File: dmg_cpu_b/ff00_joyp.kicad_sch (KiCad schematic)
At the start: 59 parts, among them P10 PAD_BIDIR_ENA_PU, P11 PAD_BIDIR_ENA_PU, P12 PAD_BIDIR_ENA_PU, P13 PAD_BIDIR_ENA_PU, P14 PAD_OUT_DIFF, P15 PAD_OUT_DIFF

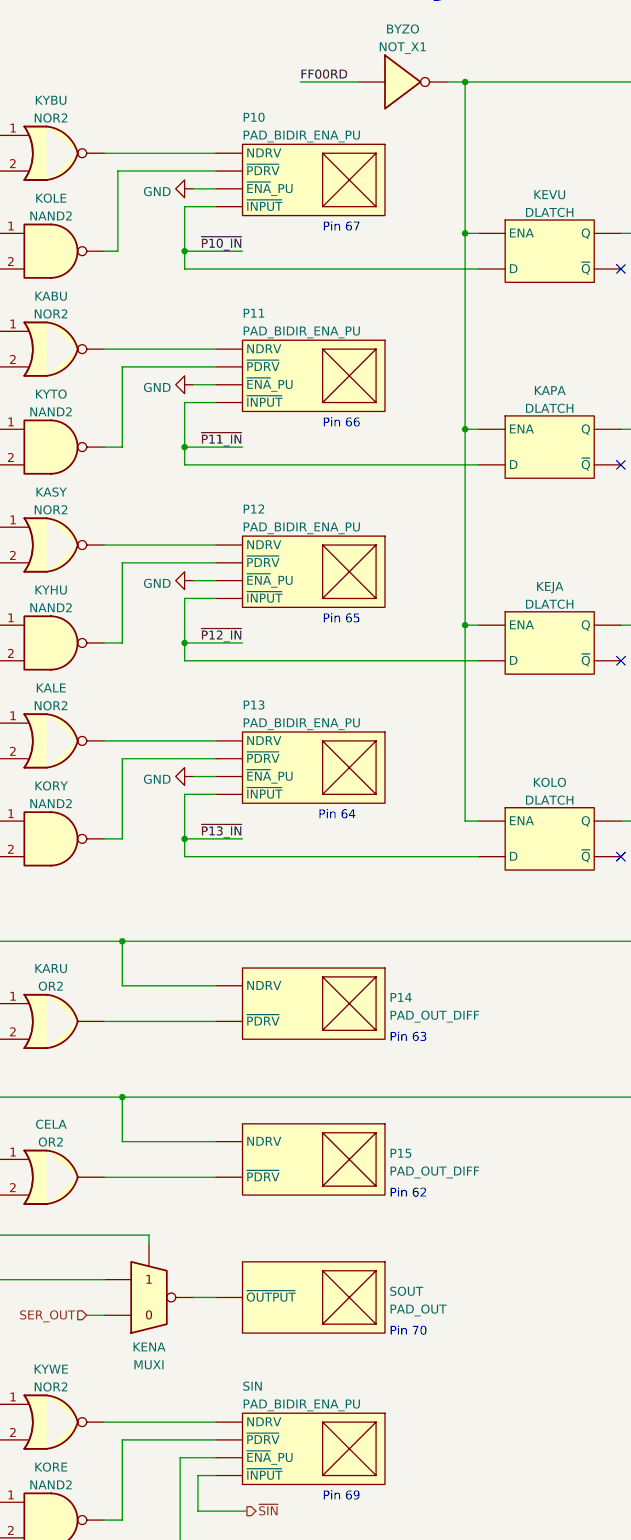
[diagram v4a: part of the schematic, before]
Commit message: Fix PAD_BIDIR* cell schematics and symbols
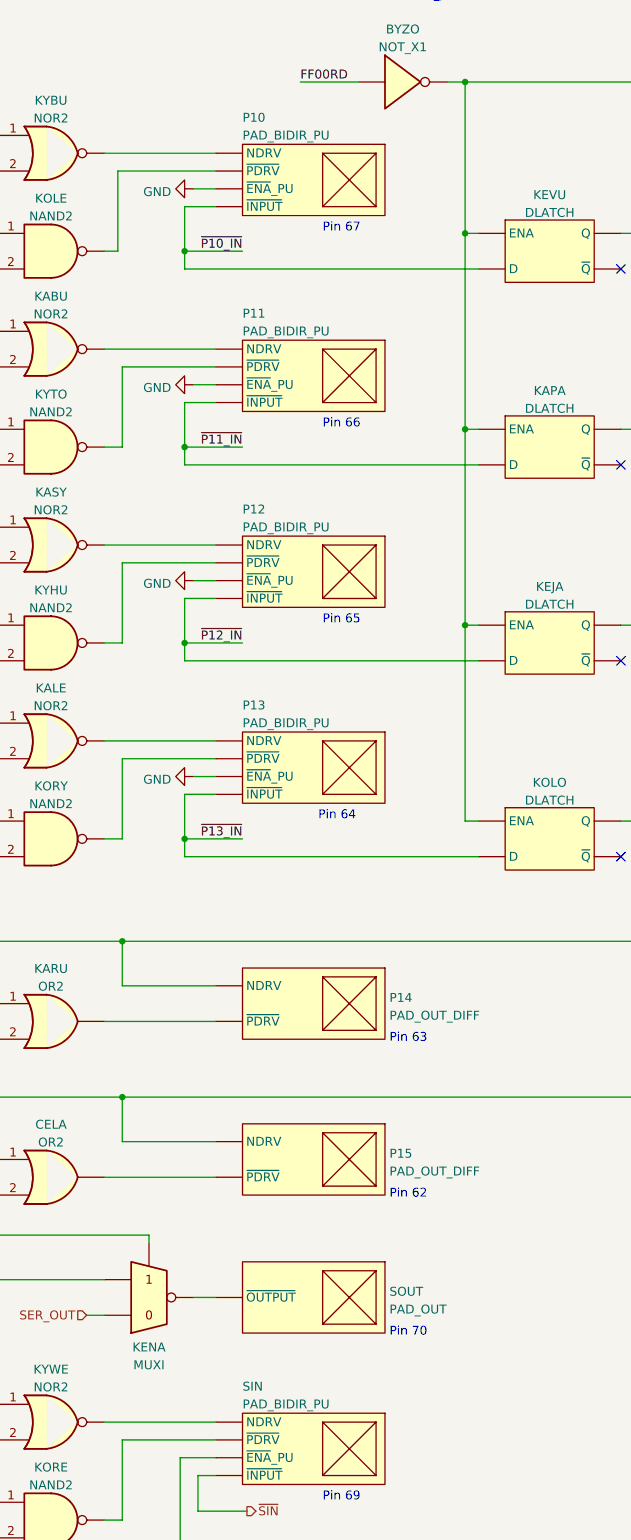
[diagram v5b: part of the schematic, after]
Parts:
- P10, P11, P12, P13, SIN: value PAD_BIDIR_ENA_PU -> PAD_BIDIR_PU; symbol DMG_CPU_Cells:PAD_BIDIR_ENA_PU -> DMG_CPU_Cells:PAD_BIDIR_PU
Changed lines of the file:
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@@
 	(title_block
 		(title "DMG-CPU B")
-		(date "2025-12-25")
+		(date "2026-02-21")
 		(rev "0.9")
 		(company "CC-BY-SA-4.0 Régis Galland & Michael Singer -- Derived work from Furrtek")
@@
 	)
 	(symbol
-		(lib_id "DMG_CPU_Cells:PAD_BIDIR_ENA_PU")
+		(lib_id "DMG_CPU_Cells:PAD_BIDIR_PU")
 		(at 277.495 128.905 0)
 		(mirror y)
@@
 			)
 		)
-		(property "Value" "PAD_BIDIR_ENA_PU"
+		(property "Value" "PAD_BIDIR_PU"
 			(at 267.335 122.555 0)
 			(effects
@@
 			)
 		)
-		(property "Datasheet" "http://iceboy.a-singer.de/doc/dmg_cells.html#pad_bidir_ena_pu"
+		(property "Datasheet" "http://iceboy.a-singer.de/doc/dmg_cells.html#pad_bidir_pu"
 			(at 277.495 137.795 0)
 			(effects
@@
 	)
 	(symbol
-		(lib_id "DMG_CPU_Cells:PAD_BIDIR_ENA_PU")
+		(lib_id "DMG_CPU_Cells:PAD_BIDIR_PU")
 		(at 277.495 254 0)
 		(mirror y)
@@
 			)
 		)
-		(property "Value" "PAD_BIDIR_ENA_PU"
+		(property "Value" "PAD_BIDIR_PU"
 			(at 267.335 247.65 0)
 			(effects
@@
 			)
 		)
-		(property "Datasheet" "http://iceboy.a-singer.de/doc/dmg_cells.html#pad_bidir_ena_pu"
+		(property "Datasheet" "http://iceboy.a-singer.de/doc/dmg_cells.html#pad_bidir_pu"
 			(at 277.495 262.89 0)
 			(effects
@@
 	)
 	(symbol
-		(lib_id "DMG_CPU_Cells:PAD_BIDIR_ENA_PU")
+		(lib_id "DMG_CPU_Cells:PAD_BIDIR_PU")
 		(at 277.495 156.845 0)
 		(mirror y)
@@
 			)
 		)
-		(property "Value" "PAD_BIDIR_ENA_PU"
+		(property "Value" "PAD_BIDIR_PU"
 			(at 267.335 150.495 0)
 			(effects
@@
 			)
 		)
-		(property "Datasheet" "http://iceboy.a-singer.de/doc/dmg_cells.html#pad_bidir_ena_pu"
+		(property "Datasheet" "http://iceboy.a-singer.de/doc/dmg_cells.html#pad_bidir_pu"
 			(at 277.495 165.735 0)
 			(effects
@@
 	)
 	(symbol
-		(lib_id "DMG_CPU_Cells:PAD_BIDIR_ENA_PU")
+		(lib_id "DMG_CPU_Cells:PAD_BIDIR_PU")
 		(at 277.495 73.025 0)
 		(mirror y)
@@
 			)
 		)
-		(property "Value" "PAD_BIDIR_ENA_PU"
+		(property "Value" "PAD_BIDIR_PU"
 			(at 267.335 66.675 0)
 			(effects
@@
 			)
 		)
-		(property "Datasheet" "http://iceboy.a-singer.de/doc/dmg_cells.html#pad_bidir_ena_pu"
+		(property "Datasheet" "http://iceboy.a-singer.de/doc/dmg_cells.html#pad_bidir_pu"
 			(at 277.495 81.915 0)
 			(effects
@@
 	)
 	(symbol
-		(lib_id "DMG_CPU_Cells:PAD_BIDIR_ENA_PU")
+		(lib_id "DMG_CPU_Cells:PAD_BIDIR_PU")
 		(at 277.495 100.965 0)
 		(mirror y)
@@
 			)
 		)
-		(property "Value" "PAD_BIDIR_ENA_PU"
+		(property "Value" "PAD_BIDIR_PU"
 			(at 267.335 94.615 0)
 			(effects
@@
 			)
 		)
-		(property "Datasheet" "http://iceboy.a-singer.de/doc/dmg_cells.html#pad_bidir_ena_pu"
+		(property "Datasheet" "http://iceboy.a-singer.de/doc/dmg_cells.html#pad_bidir_pu"
 			(at 277.495 109.855 0)
 			(effects
